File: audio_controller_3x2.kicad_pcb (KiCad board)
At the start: 2 copper layers, 69.8 x 40.6 mm, 1 part

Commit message: Progress towards v1.0.
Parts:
- added C1: 0.1uF, audio_controller_3x2:SM1210, B.Cu at (125.7, 99.1)
- added C2: 2.2uF, audio_controller_3x2:SM1210, B.Cu at (135.9, 99.1)
- added C3: 0.1uF, audio_controller_3x2:SM1210, B.Cu at (141.0, 99.1)
- added C4: 0.15uF, audio_controller_3x2:SM1210, B.Cu at (120.7, 99.1)
- added C5: 2.2uF, audio_controller_3x2:SM1210, B.Cu at (107.3, 78.7)
- added C6: 0.1uF, audio_controller_3x2:SM1210, B.Cu at (112.4, 78.7)
- added C7: 2.2uF, audio_controller_3x2:SM1210, B.Cu at (122.6, 78.7)
- added J1: AUDIO_JACK_3.5MM, audio_controller_3x2:AUDIO_JACK_3.5MM_3PIN, B.Cu at (155.6, 88.9)
- added L1: 600, audio_controller_3x2:SM1210, B.Cu at (130.8, 99.1)
- added R1: 2.21k, audio_controller_3x2:SM1210, B.Cu at (107.3, 88.9)
- added R2: 2.21k, audio_controller_3x2:SM1210, B.Cu at (112.4, 88.9)
- added U1: SGTL5000, audio_controller_3x2:QFN-5x5-32, B.Cu at (130.8, 88.9)
- added U2: AP7313_1.5V, audio_controller_3x2:SOT-23-3, B.Cu at (117.5, 78.7)
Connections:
- MDB1 pad 11: (no net) -> /MCLK
- MDB1 pad 13: (no net) -> /I2SRX
- MDB1 pad 18: (no net) -> /SDA
- MDB1 pad 19: (no net) -> /SCL
- MDB1 pad 22: (no net) -> /I2STX
- MDB1 pad 23: (no net) -> /LRCLK
- MDB1 pad 3V3: (no net) -> +3V3
- MDB1 pad 9: (no net) -> /BCLK
- MDB1 pad GND: (no net) -> GND
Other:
- net class POWER: trace_width 0.8128 -> 0.4064
- board text added: "Janelia Modular Device audio_controller part_number: 1151 03/2017 ver 1.0 3x2"
- board text removed: "Janelia Modular Device audio_controller part_number: 1000 02/2017 ver 1.0 3x2"

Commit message: Finished version 1.0.
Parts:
- moved C5 23.5 mm to (130.8, 78.7)
- moved C7 23.5 mm to (146.1, 78.7)
- moved U2 23.5 mm to (141.0, 78.7)
- moved C6 23.5 mm to (135.9, 78.7)
- moved R1 21.0 mm to (125.7, 78.7)
- moved R2 13.1 mm to (120.7, 78.7)
- moved C2 10.2 mm to (146.1, 99.1)
- moved C1 5.08 mm to (130.8, 99.1)
- moved C4 5.08 mm to (125.7, 99.1)
- moved L1 5.08 mm to (135.9, 99.1)
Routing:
- net +3V3: track 0.00 -> 137.9 mm
- net GND: track 0.00 -> 119.0 mm
- net /SDA: track 0.00 -> 71.8 mm
- net /LRCLK: track 0.00 -> 55.9 mm
- net /I2STX: track 0.00 -> 46.2 mm
- net /SCL: track 0.00 -> 41.6 mm
- net /I2SRX: track 0.00 -> 26.3 mm
- net +1V5: track 0.00 -> 25.0 mm
- net /BCLK: track 0.00 -> 22.9 mm, vias 0 -> 1
- net /HP_VGND: track 0.00 -> 21.0 mm
- net /MCLK: track 0.00 -> 21.0 mm, vias 0 -> 1
- net Net-(C2-Pad1): track 0.00 -> 20.5 mm
- net /HP_R: track 0.00 -> 18.4 mm
- net /HP_L: track 0.00 -> 16.4 mm, vias 0 -> 2
- net Net-(C4-Pad1): track 0.00 -> 15.1 mm
- added copper zone on B.Cu, net +3V3
- added copper zone on F.Cu, net GND
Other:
- net class GND: trace_width 0.4064 -> 0.3048
- net class POWER: clearance 0.254 -> 0.1016; trace_width 0.4064 -> 0.3048
- net class SIGNAL: trace_width 0.4064 -> 0.254
- net class SUPERPOWER: clearance 0.254 -> 0.1016; trace_width 1.2192 -> 0.4064
- rule trace_min: 0.254 -> 0.2032
- board text added: "Stereo Output 3.5mm 1/8" Mini Plug"

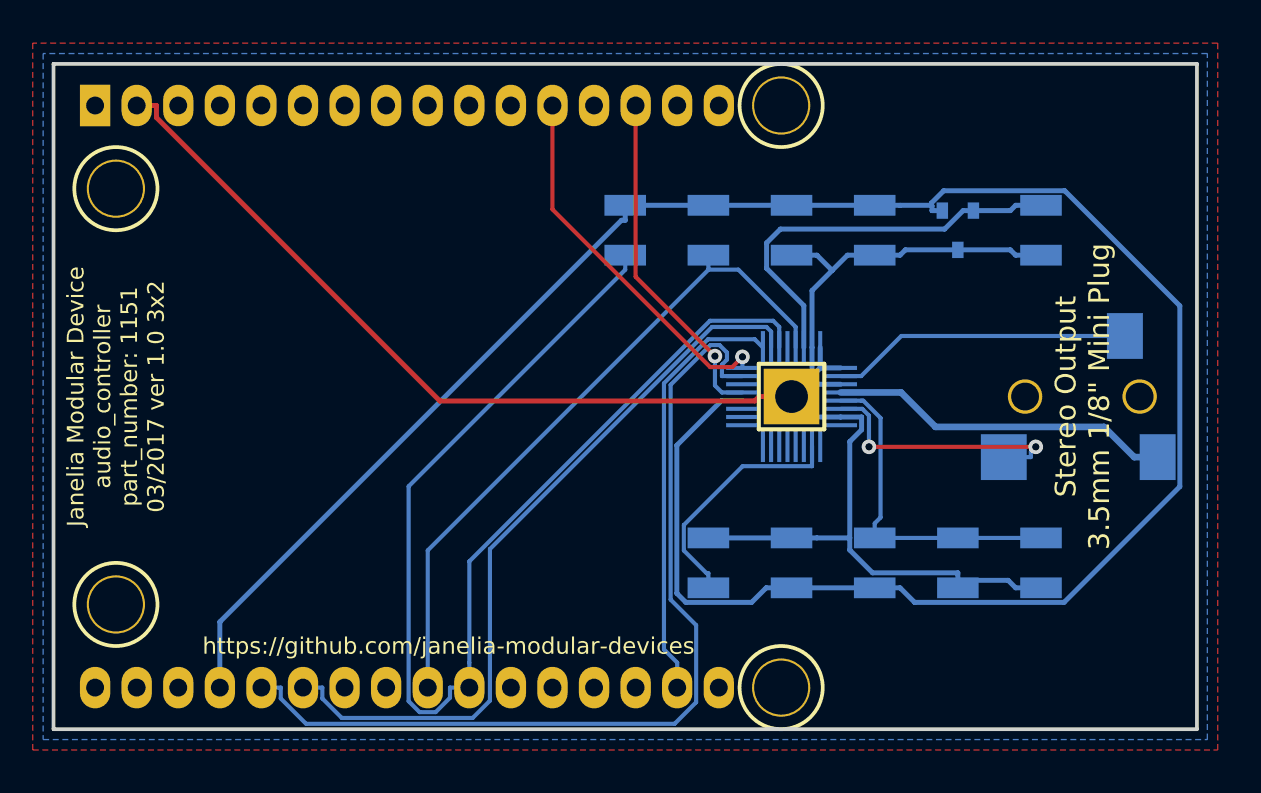
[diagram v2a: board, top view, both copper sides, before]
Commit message: Moved edge positions.
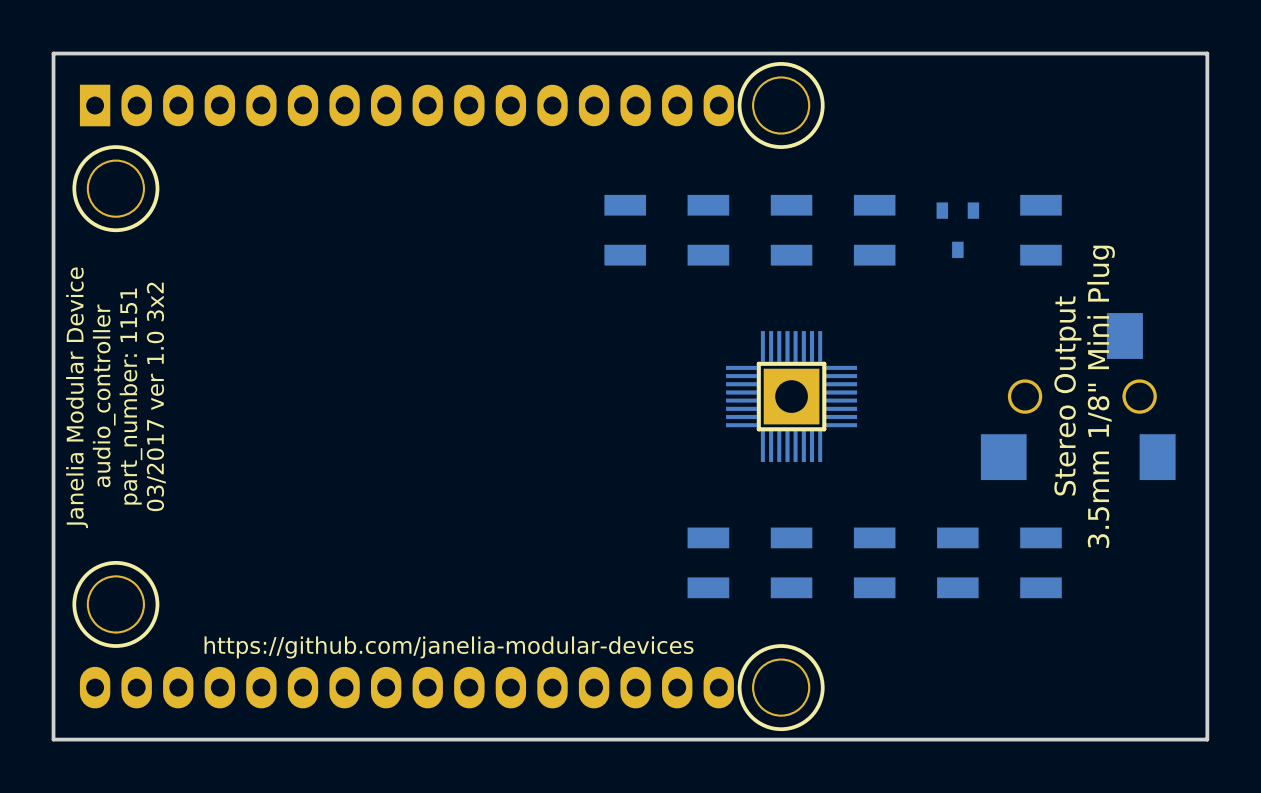
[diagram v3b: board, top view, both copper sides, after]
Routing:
- net +3V3: track 137.9 -> 0.00 mm
- net GND: track 119.0 -> 0.00 mm
- net /SDA: track 71.8 -> 0.00 mm
- net /LRCLK: track 55.9 -> 0.00 mm
- net /I2STX: track 46.2 -> 0.00 mm
- net /SCL: track 41.6 -> 0.00 mm
- net /I2SRX: track 26.3 -> 0.00 mm
- net +1V5: track 25.0 -> 0.00 mm
- net /BCLK: track 22.9 -> 0.00 mm, vias 1 -> 0
- net /HP_VGND: track 21.0 -> 0.00 mm
- net /MCLK: track 21.0 -> 0.00 mm, vias 1 -> 0
- net Net-(C2-Pad1): track 20.5 -> 0.00 mm
- net /HP_R: track 18.4 -> 0.00 mm
- net /HP_L: track 16.4 -> 0.00 mm, vias 2 -> 0
- net Net-(C4-Pad1): track 15.1 -> 0.00 mm
- removed copper zone on B.Cu, net +3V3
- removed copper zone on F.Cu, net GND
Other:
- board size 69.8 x 40.6 mm -> 70.5 x 41.9 mm

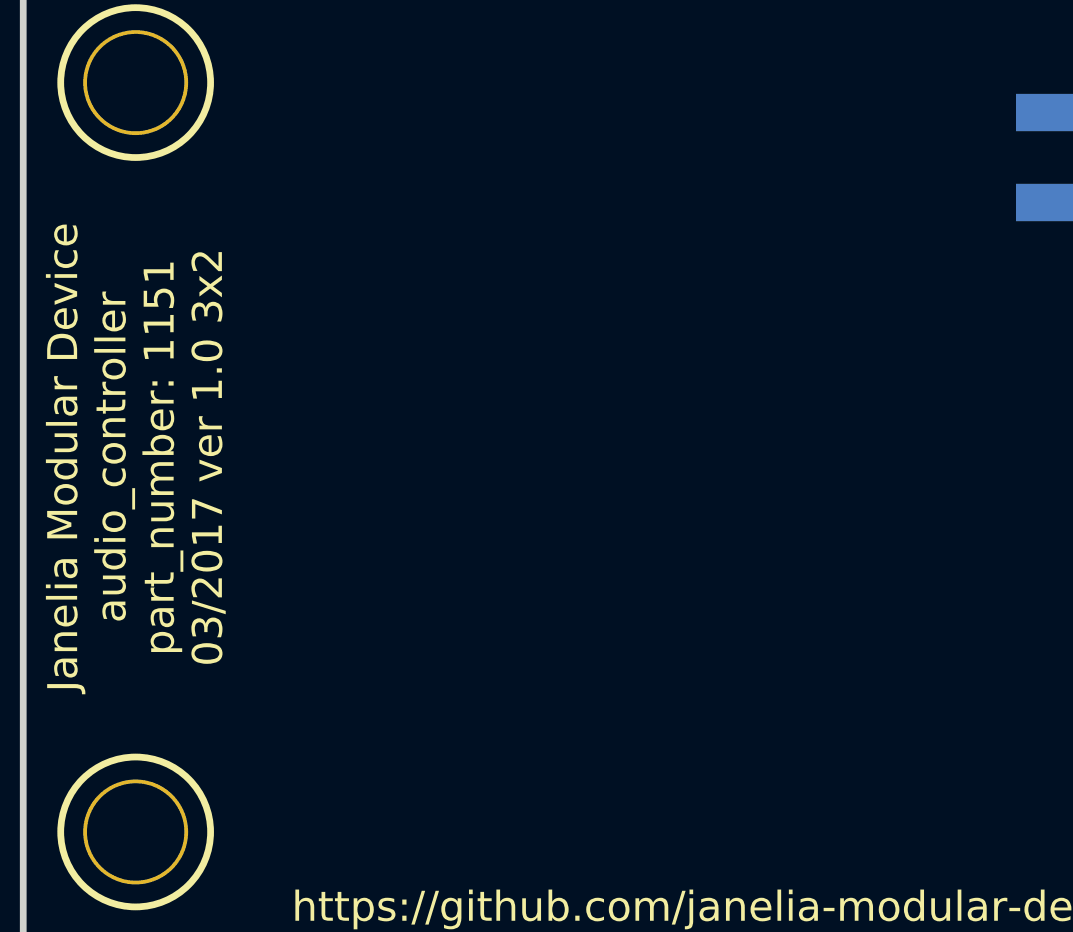
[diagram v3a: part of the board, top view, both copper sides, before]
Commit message: Added LM48310.
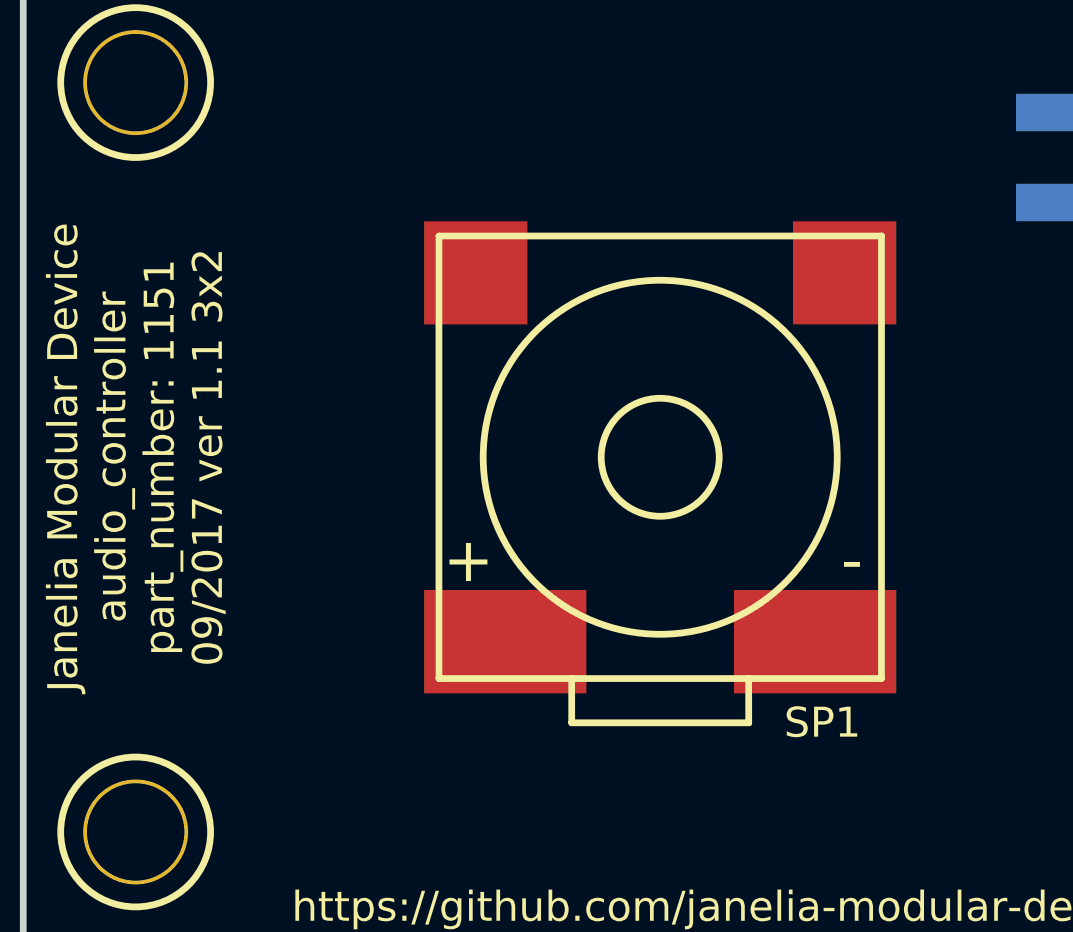
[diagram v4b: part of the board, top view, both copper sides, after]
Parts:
- added SP1: SPEAKER_8OHM_300MW, audio_controller_3x2:SPEAKER_8OHM_300MW, F.Cu at (107.3, 88.9)
- L1: value 600 -> 600@100MHz
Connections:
- MDB1 pad 10: (no net) -> Net-(MDB1-Pad10)
- MDB1 pad 12: (no net) -> Net-(MDB1-Pad12)
- MDB1 pad 14: (no net) -> Net-(MDB1-Pad14)
- MDB1 pad 15: (no net) -> Net-(MDB1-Pad15)
- MDB1 pad 16: (no net) -> Net-(MDB1-Pad16)
- MDB1 pad 17: (no net) -> Net-(MDB1-Pad17)
- MDB1 pad 2: (no net) -> Net-(MDB1-Pad2)
- MDB1 pad 20: (no net) -> Net-(MDB1-Pad20)
- MDB1 pad 21: (no net) -> Net-(MDB1-Pad21)
- MDB1 pad 24: (no net) -> Net-(MDB1-Pad24)
- MDB1 pad 25: (no net) -> Net-(MDB1-Pad25)
- MDB1 pad 28: (no net) -> Net-(MDB1-Pad28)
- MDB1 pad 29: (no net) -> Net-(MDB1-Pad29)
- MDB1 pad 3: (no net) -> Net-(MDB1-Pad3)
- MDB1 pad 30: (no net) -> Net-(MDB1-Pad30)
- MDB1 pad 4: (no net) -> Net-(MDB1-Pad4)
- MDB1 pad 5: (no net) -> Net-(MDB1-Pad5)
- MDB1 pad 6: (no net) -> Net-(MDB1-Pad6)
- MDB1 pad AGND: (no net) -> Net-(MDB1-PadAGND)
- MDB1 pad AREF: (no net) -> Net-(MDB1-PadAREF)
- MDB1 pad DAC: (no net) -> Net-(MDB1-PadDAC)
- MDB1 pad VDD: (no net) -> VDD
- MDB1 pad VEE: (no net) -> VEE
- U1 pad 11: (no net) -> Net-(U1-Pad11)
- U1 pad 12: (no net) -> Net-(U1-Pad12)
- U1 pad 13: (no net) -> Net-(U1-Pad13)
- U1 pad 14: (no net) -> Net-(U1-Pad14)
- U1 pad 15: (no net) -> Net-(U1-Pad15)
- U1 pad 16: (no net) -> Net-(U1-Pad16)
- U1 pad 18: (no net) -> Net-(U1-Pad18)
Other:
- net class Default: trace_width 0.254 -> 0.25
- board text added: "Janelia Modular Device audio_controller part_number: 1151 09/2017 ver 1.1 3x2"
- board text removed: "Janelia Modular Device audio_controller part_number: 1151 03/2017 ver 1.0 3x2"

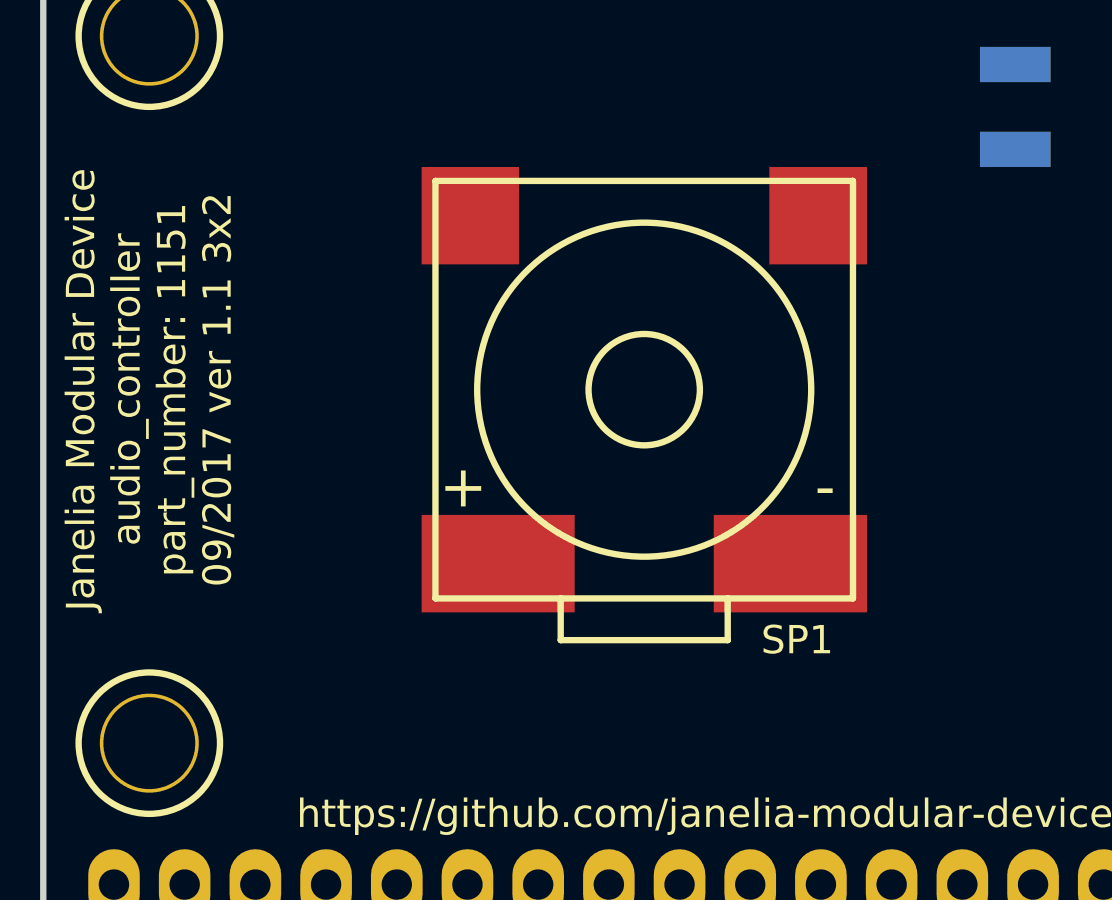
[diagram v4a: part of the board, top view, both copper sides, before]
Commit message: Added speaker and amplifier.
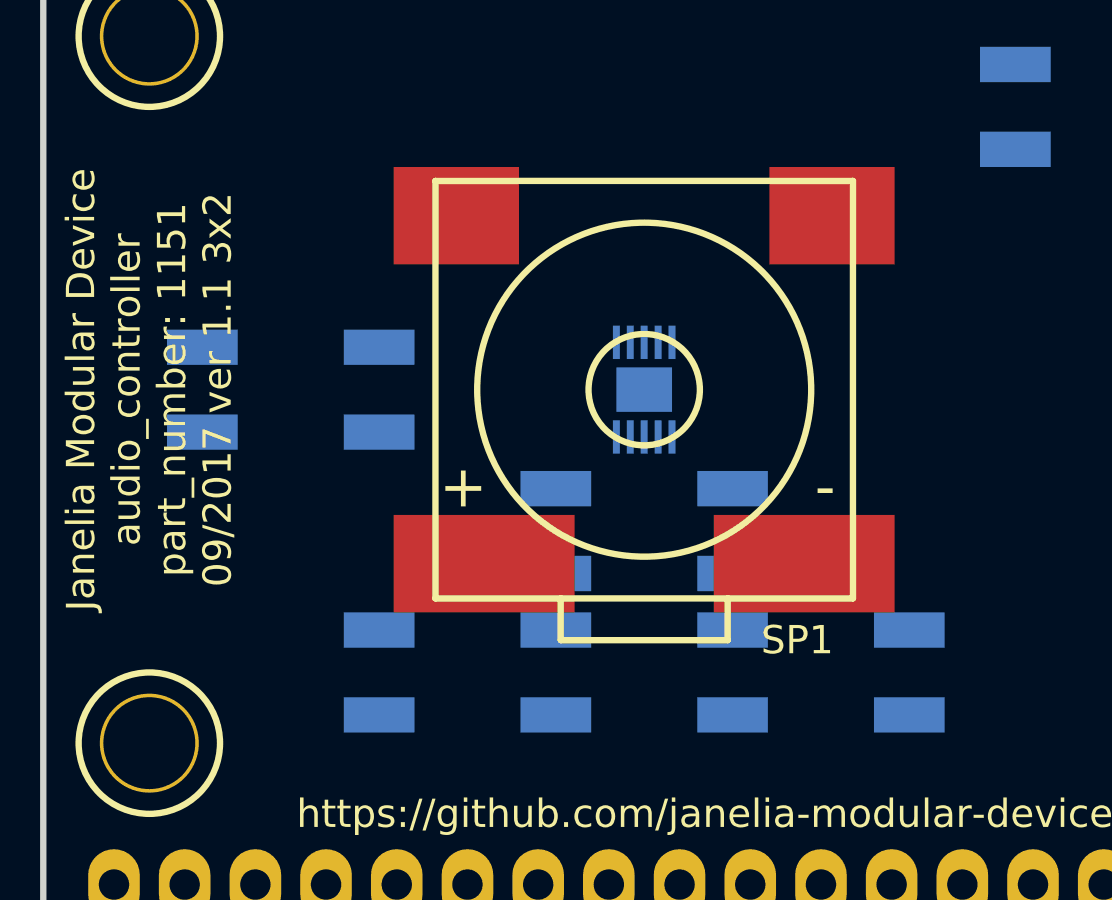
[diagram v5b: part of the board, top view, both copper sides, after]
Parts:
- added C10: 1uF, audio_controller_3x2:SM1210, B.Cu at (110.5, 94.0)
- added C11: 1uF, audio_controller_3x2:SM1210, B.Cu at (104.1, 94.0)
- added C12: 2.2uF, audio_controller_3x2:SM1210, B.Cu at (91.4, 88.9)
- added C13: 0.1uF, audio_controller_3x2:SM1210, B.Cu at (97.8, 88.9)
- added C8: 3.3nF, audio_controller_3x2:SM1210, B.Cu at (116.8, 99.1)
- added C9: 3.3nF, audio_controller_3x2:SM1210, B.Cu at (97.8, 99.1)
- added R3: 2.21k, audio_controller_3x2:SM1210, B.Cu at (110.5, 99.1)
- added R4: 2.21k, audio_controller_3x2:SM1210, B.Cu at (104.1, 99.1)
- added U3: LM48310, audio_controller_3x2:10-WFDFN_EXPOSED_PAD, B.Cu at (107.3, 88.9)
- L1: value 600@100MHz -> 600
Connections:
- J1 pad 1: /HP_VGND -> (no net)
- MDB1 pad 10: Net-(MDB1-Pad10) -> (no net)
- MDB1 pad 12: Net-(MDB1-Pad12) -> (no net)
- MDB1 pad 14: Net-(MDB1-Pad14) -> (no net)
- MDB1 pad 15: Net-(MDB1-Pad15) -> (no net)
- MDB1 pad 16: Net-(MDB1-Pad16) -> (no net)
- MDB1 pad 17: Net-(MDB1-Pad17) -> (no net)
- MDB1 pad 2: Net-(MDB1-Pad2) -> (no net)
- MDB1 pad 20: Net-(MDB1-Pad20) -> (no net)
- MDB1 pad 21: Net-(MDB1-Pad21) -> (no net)
- MDB1 pad 24: Net-(MDB1-Pad24) -> (no net)
- MDB1 pad 25: Net-(MDB1-Pad25) -> (no net)
- MDB1 pad 28: Net-(MDB1-Pad28) -> (no net)
- MDB1 pad 29: Net-(MDB1-Pad29) -> (no net)
- MDB1 pad 3: Net-(MDB1-Pad3) -> (no net)
- MDB1 pad 30: Net-(MDB1-Pad30) -> (no net)
- MDB1 pad 4: Net-(MDB1-Pad4) -> (no net)
- MDB1 pad 5: Net-(MDB1-Pad5) -> (no net)
- MDB1 pad 6: Net-(MDB1-Pad6) -> /SPEAKER_ENABLE
- MDB1 pad AGND: Net-(MDB1-PadAGND) -> /AGND
- MDB1 pad AREF: Net-(MDB1-PadAREF) -> (no net)
- MDB1 pad DAC: Net-(MDB1-PadDAC) -> /DAC
- MDB1 pad VDD: VDD -> (no net)
- SP1 pad 1: Net-(SP1-Pad1) -> /AMP+
- SP1 pad 2: Net-(SP1-Pad2) -> /AMP-
- U1 pad 11: Net-(U1-Pad11) -> (no net)
- U1 pad 12: Net-(U1-Pad12) -> (no net)
- U1 pad 13: Net-(U1-Pad13) -> (no net)
- U1 pad 14: Net-(U1-Pad14) -> (no net)
- U1 pad 15: Net-(U1-Pad15) -> (no net)
- U1 pad 16: Net-(U1-Pad16) -> (no net)
- U1 pad 18: Net-(U1-Pad18) -> (no net)
- U1 pad 4: /HP_VGND -> GND

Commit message: Finished v1.1.
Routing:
- net GND: track 0.00 -> 148.0 mm, vias 0 -> 3
- net +3V3: track 0.00 -> 134.9 mm
- net /SDA: track 0.00 -> 87.9 mm
- net VEE: track 0.00 -> 64.4 mm
- net /SCL: track 0.00 -> 52.8 mm, vias 0 -> 1
- net /I2STX: track 0.00 -> 39.8 mm, vias 0 -> 1
- net /LRCLK: track 0.00 -> 39.7 mm, vias 0 -> 1
- net /MCLK: track 0.00 -> 32.3 mm
- net /I2SRX: track 0.00 -> 30.2 mm, vias 0 -> 1
- net Net-(C2-Pad1): track 0.00 -> 29.0 mm
- net /AGND: track 0.00 -> 28.5 mm
- net +1V5: track 0.00 -> 25.1 mm
- net /SPEAKER_ENABLE: track 0.00 -> 23.9 mm
- net /BCLK: track 0.00 -> 22.3 mm
- net /DAC: track 0.00 -> 19.3 mm
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- added copper zone on B.Cu, net GND
- added copper zone on F.Cu, net GND
